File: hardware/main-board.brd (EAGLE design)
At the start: 100 x 80 mm, 8 parts

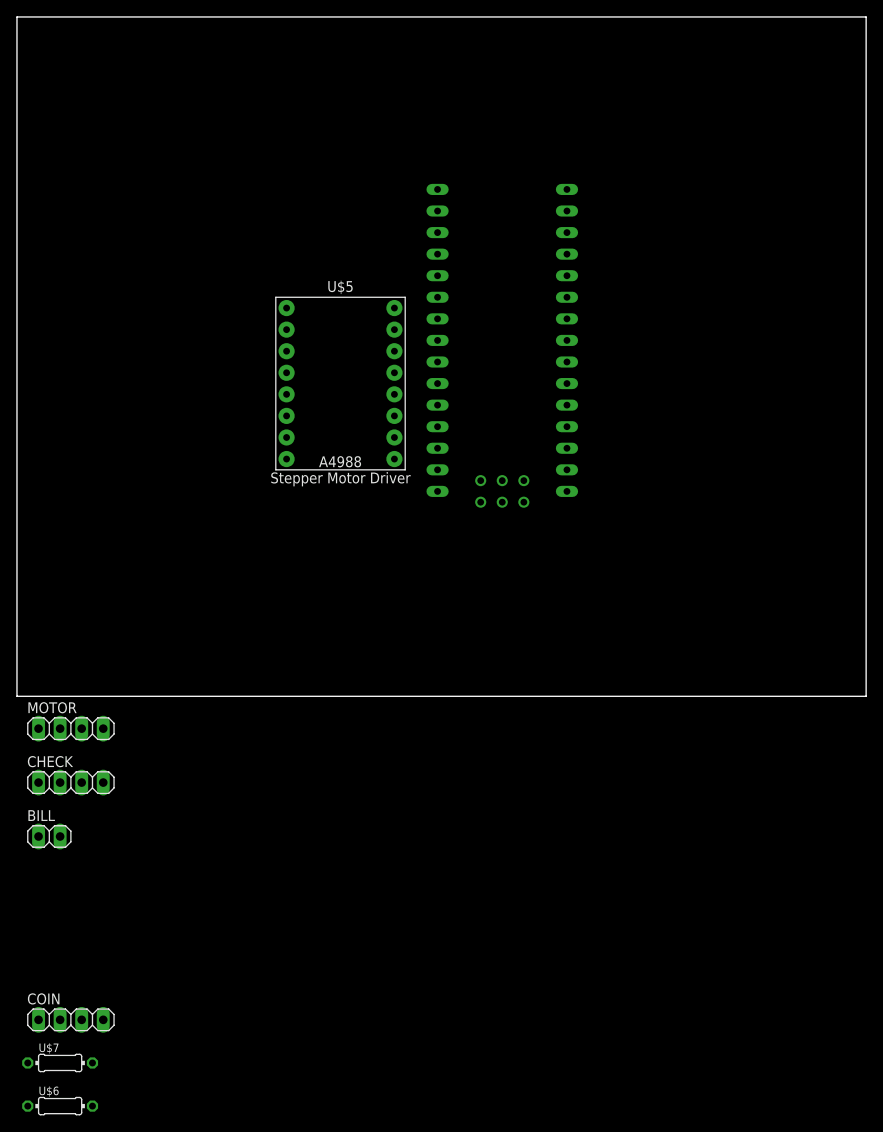
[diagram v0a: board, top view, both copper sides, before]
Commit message: fix board layout - motor outputs corrected - pullup resistor corrected on coin acceptor
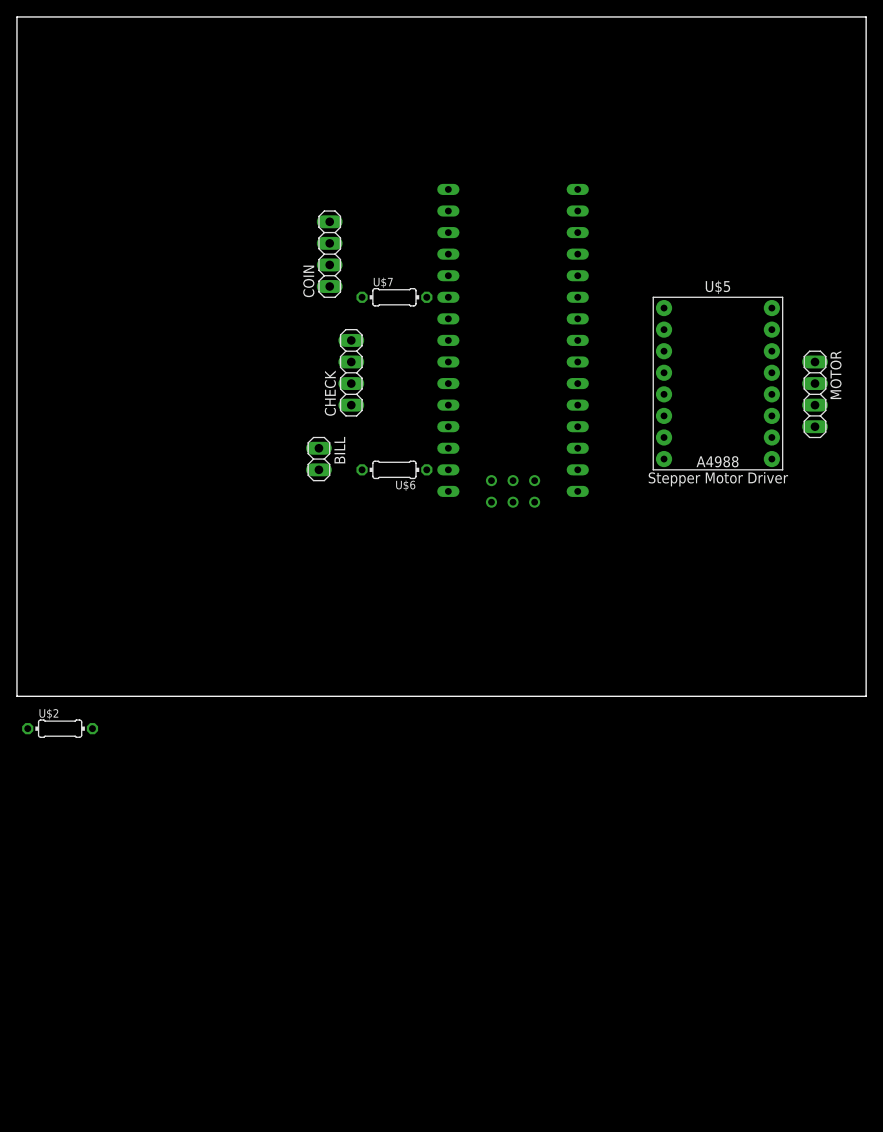
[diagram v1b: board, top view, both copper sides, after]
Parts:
- added U$2: R-US, mcp:0204/7
- moved U$7 98.4 mm to (44.5, 47.0)
- moved MOTOR 96.1 mm to (94.0, 35.6), turned to 270 degrees
- moved COIN 95.2 mm to (36.8, 52.1), turned to 90 degrees
- moved U$6 84.6 mm to (44.5, 26.7), turned to 180 degrees
- moved CHECK 58.5 mm to (39.4, 38.1), turned to 90 degrees
- moved BILL 54.6 mm to (35.6, 27.9), turned to 270 degrees
- moved U$5 44.4 mm to (82.5, 36.8)
- moved U$1 1.27 mm to (61.0, 33.0)
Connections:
- removed net N$5: MOTOR.2, U$5.2A
- removed net N$6: MOTOR.3, U$5.1A
- new net N$1: MOTOR.2, U$5.1A
- new net N$2: MOTOR.3, U$5.2A
- net +5V: now also U$2.1
- net CHK_DETECT: now also U$2.2
